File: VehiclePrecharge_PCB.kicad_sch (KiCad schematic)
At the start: 43 parts, among them J1 USB_B, J2 Conn_01x02, J3 Conn_01x02, J4 Main, J5 Conn_01x02, K1 2-1904058-5, Q1 BC847BS, Q2 SSM3J328R LF, SW1 SW_SPDT, U12 LT218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

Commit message: More schematic completed
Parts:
- removed J2, J3: Conn_01x02, symbol Connector_Generic:Conn_01x02
- R11: value 3k -> 10k
- R7: value 220R -> R_small
- U12, U4: value LT218 -> AQY212
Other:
- sheet PWM Economizer1 ports: added Control; removed none
- sheet PWM Economizer2 ports: added Control; removed none
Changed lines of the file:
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@@
     (effects (font (size 1.27 1.27)) (justify left bottom))
-  )
-  (global_label "Shutdown Loop" (shape input) (at 365.76 172.72 180) (fields_autoplaced)
-    (effects (font (size 1.27 1.27)) (justify right))
-    (property "Intersheetrefs" "${INTERSHEET_REFS}" (at 348.6064 172.72 0)
-      (effects (font (size 1.27 1.27)) (justify right) hide)
-    )
   )
   (global_label "SD GND" (shape bidirectional) (at 100.33 204.47 180) (fields_autoplaced)
@@
     )
   )
-  (global_label "AIR- Control" (shape input) (at 274.32 175.26 180) (fields_autoplaced)
+  (global_label "AIR- Control" (shape input) (at 288.29 175.26 180) (fields_autoplaced)
     (effects (font (size 1.27 1.27)) (justify right))
-    (property "Intersheetrefs" "${INTERSHEET_REFS}" (at 259.2223 175.26 0)
+    (property "Intersheetrefs" "${INTERSHEET_REFS}" (at 273.1923 175.26 0)
       (effects (font (size 1.27 1.27)) (justify right) hide)
     )
@@
     )
   )
-  (global_label "Shutdown Loop" (shape input) (at 365.76 151.13 180) (fields_autoplaced)
-    (effects (font (size 1.27 1.27)) (justify right))
-    (property "Intersheetrefs" "${INTERSHEET_REFS}" (at 348.6064 151.13 0)
-      (effects (font (size 1.27 1.27)) (justify right) hide)
-    )
-  )
   (global_label "ALV+" (shape input) (at 38.1 198.12 180) (fields_autoplaced)
     (effects (font (size 1.27 1.27)) (justify right))
@@
     )
   )
-  (global_label "AIR+ Control" (shape input) (at 274.32 152.4 180) (fields_autoplaced)
+  (global_label "AIR+ Control" (shape input) (at 288.29 152.4 180) (fields_autoplaced)
     (effects (font (size 1.27 1.27)) (justify right))
-    (property "Intersheetrefs" "${INTERSHEET_REFS}" (at 259.2223 152.4 0)
+    (property "Intersheetrefs" "${INTERSHEET_REFS}" (at 273.1923 152.4 0)
       (effects (font (size 1.27 1.27)) (justify right) hide)
     )
@@
       (effects (font (size 1.27 1.27)) (justify left))
     )
-    (property "Value" "220R" (at 38.1 269.875 0)
+    (property "Value" "R_small" (at 38.1 269.875 0)
       (effects (font (size 1.27 1.27)) (justify left))
     )
@@
         (path "/3146712d-38b0-45c4-b96b-45a0a31bd3ed"
           (reference "R7") (unit 1)
-        )
-      )
-    )
-  )
-  (symbol (lib_id "Connector_Generic:Conn_01x02") (at 370.84 151.13 0) (unit 1)
-    (in_bom yes) (on_board yes) (dnp no) (fields_autoplaced)
-    (property "Reference" "J2" (at 373.38 151.765 0)
-      (effects (font (size 1.27 1.27)) (justify left))
-    )
-    (property "Value" "Conn_01x02" (at 373.38 154.305 0)
-      (effects (font (size 1.27 1.27)) (justify left))
-    )
-    (property "Footprint" "" (at 370.84 151.13 0)
-      (effects (font (size 1.27 1.27)) hide)
-    )
-    (property "Datasheet" "~" (at 370.84 151.13 0)
-      (effects (font (size 1.27 1.27)) hide)
-    )
-    (pin "1")
-    (pin "2")
-    (instances
-      (project "VehiclePrecharge_PCB"
-        (path "/3146712d-38b0-45c4-b96b-45a0a31bd3ed"
-          (reference "J2") (unit 1)
         )
       )
@@
       (effects (font (size 1.27 1.27)))
     )
-    (property "Value" "LT218" (at 279.4 60.96 0)
+    (property "Value" "AQY212" (at 279.4 60.96 0)
       (effects (font (size 1.27 1.27)))
     )
@@
         (path "/e63e39d7-6ac0-4ffd-8aa3-1841a4541b55"
           (reference "D7") (unit 1)
-        )
-      )
-    )
-  )
-  (symbol (lib_id "Connector_Generic:Conn_01x02") (at 370.84 172.72 0) (unit 1)
-    (in_bom yes) (on_board yes) (dnp no) (fields_autoplaced)
-    (property "Reference" "J3" (at 373.38 173.355 0)
-      (effects (font (size 1.27 1.27)) (justify left))
-    )
-    (property "Value" "Conn_01x02" (at 373.38 175.895 0)
-      (effects (font (size 1.27 1.27)) (justify left))
-    )
-    (property "Footprint" "" (at 370.84 172.72 0)
-      (effects (font (size 1.27 1.27)) hide)
-    )
-    (property "Datasheet" "~" (at 370.84 172.72 0)
-      (effects (font (size 1.27 1.27)) hide)
-    )
-    (pin "1")
-    (pin "2")
-    (instances
-      (project "VehiclePrecharge_PCB"
-        (path "/3146712d-38b0-45c4-b96b-45a0a31bd3ed"
-          (reference "J3") (unit 1)
         )
       )
@@
       (effects (font (size 1.27 1.27)))
     )
-    (property "Value" "3k" (at 158.75 53.34 90)
+    (property "Value" "10k" (at 158.75 53.34 90)
       (effects (font (size 1.27 1.27)))
     )
@@
       (effects (font (size 1.27 1.27)))
     )
-    (property "Value" "LT218" (at 45.72 255.27 0)
+    (property "Value" "AQY212" (at 45.72 255.27 0)
       (effects (font (size 1.27 1.27)))
     )
@@
       (effects (font (size 1.27 1.27)) (justify left top))
     )
+    (pin "Control" input (at 288.29 175.26 180)
+      (effects (font (size 1.27 1.27)) (justify left))
+    )
     (instances
       (project "VehiclePrecharge_PCB"
@@
       (effects (font (size 1.27 1.27)) (justify left top))
     )
-    (instances
+    (pin "Control" input (at 288.29 152.4 180)
+      (effects (font (size 1.27 1.27)) (justify left))
+    )
+    (instances

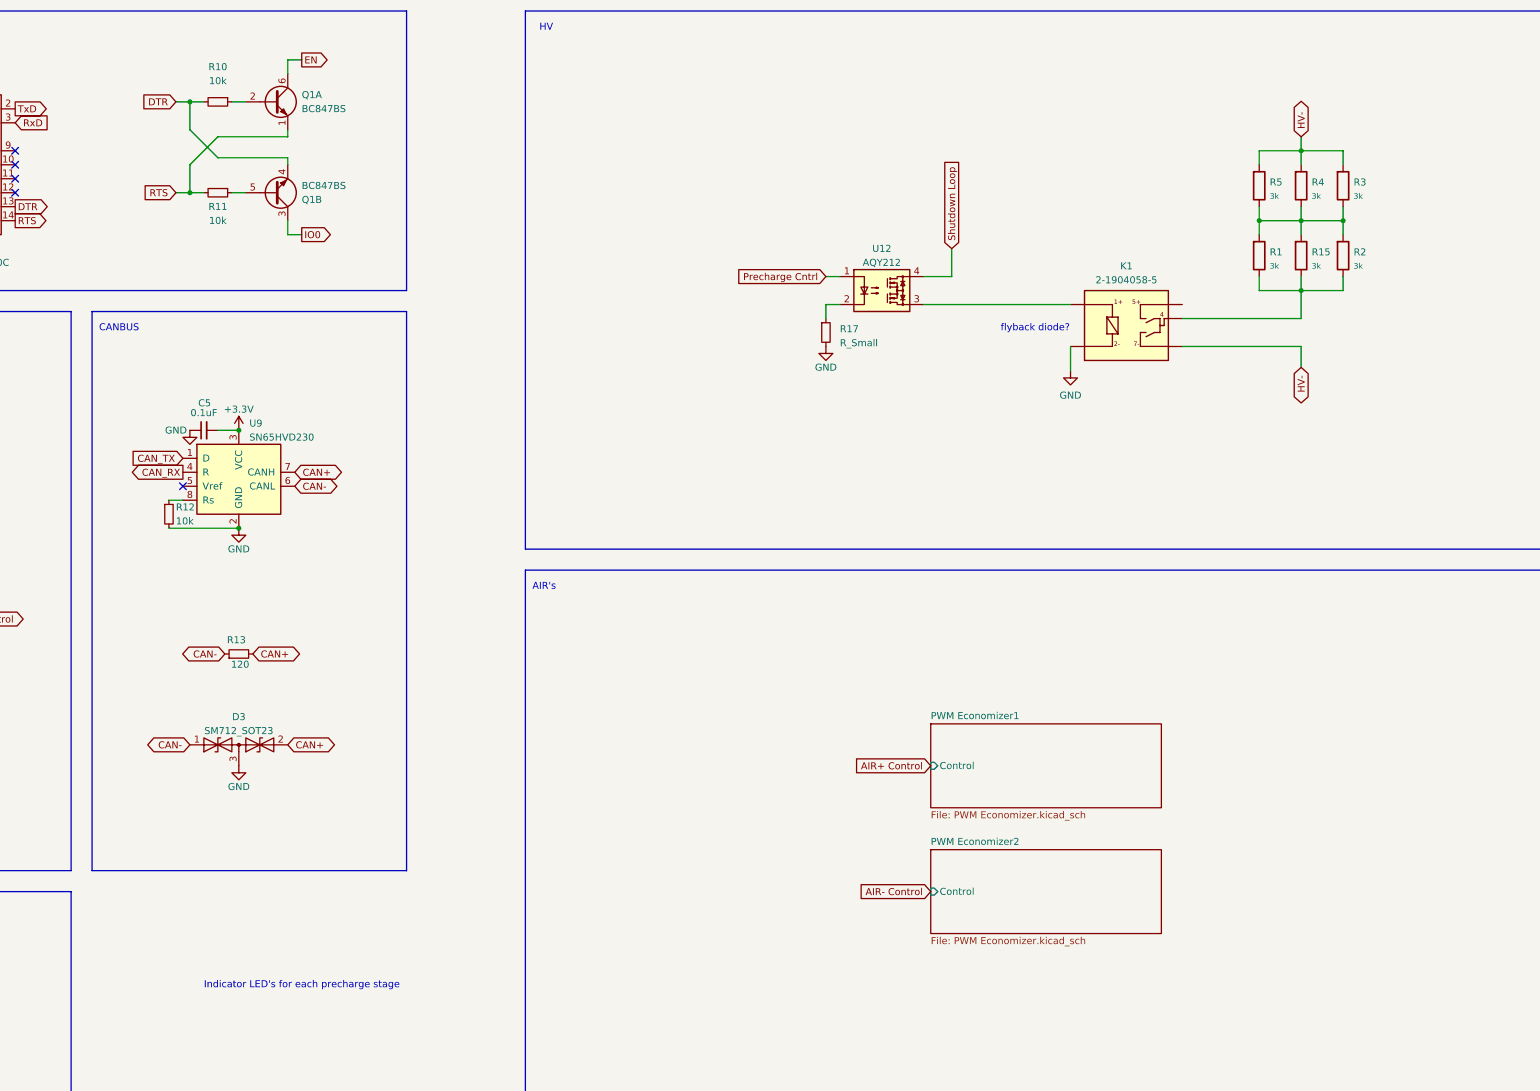
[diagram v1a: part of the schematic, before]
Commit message: Changed to DRV110A
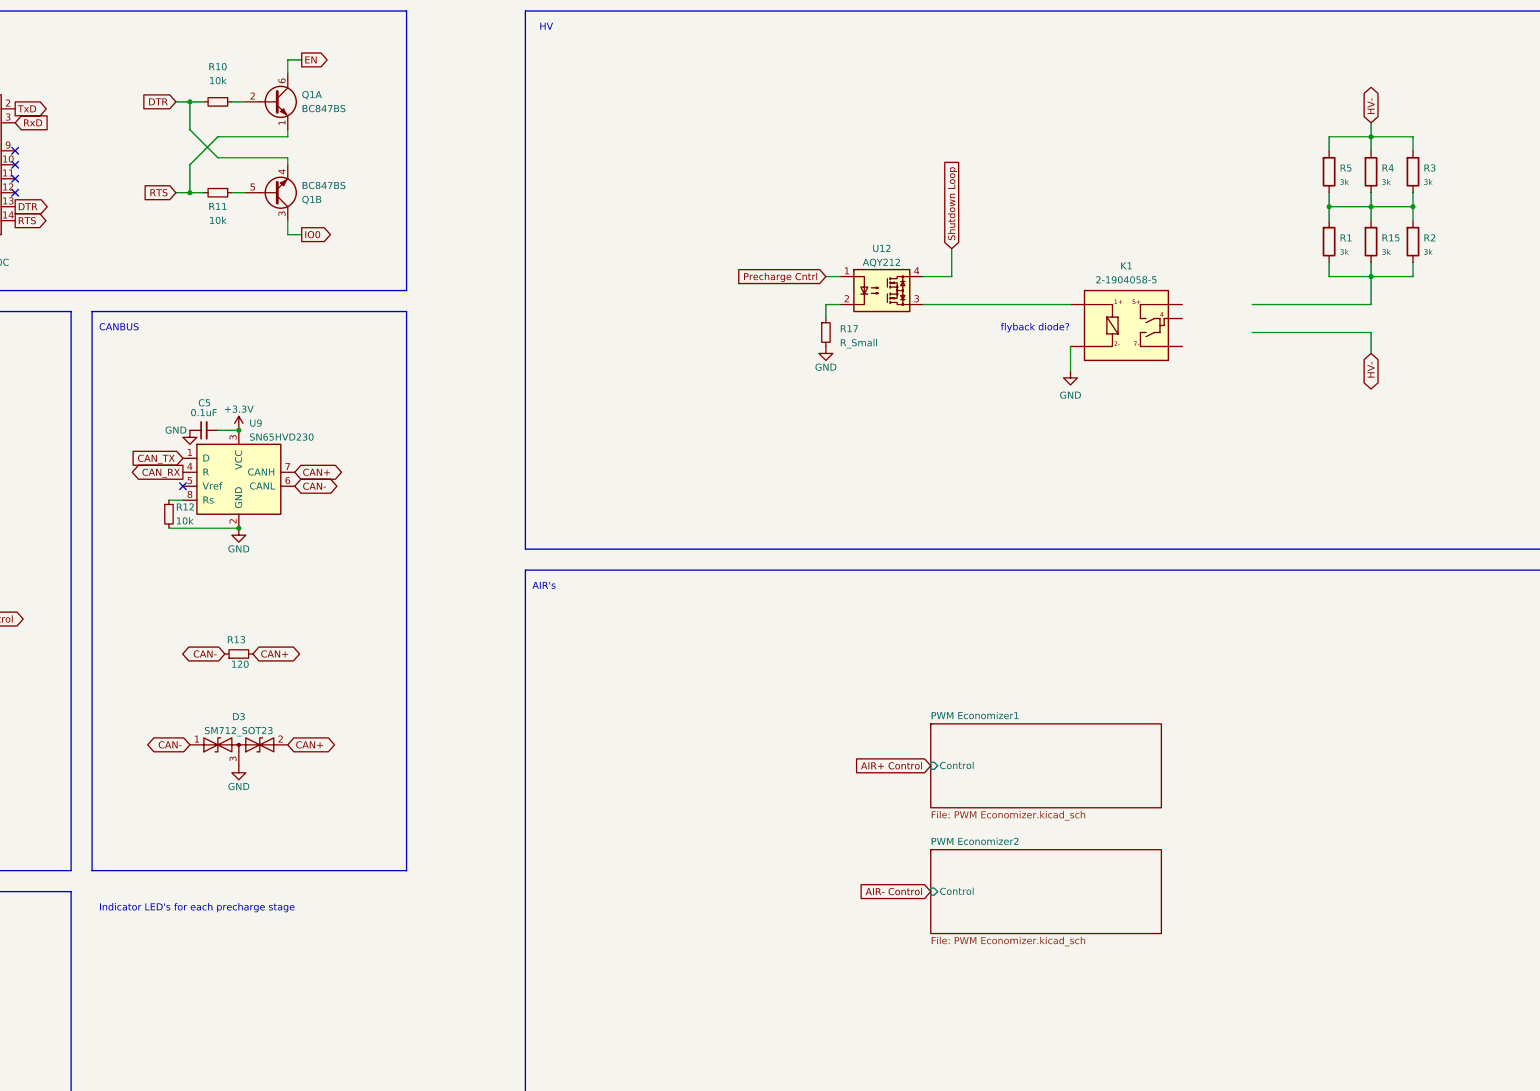
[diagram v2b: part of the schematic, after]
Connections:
- net HV-: no longer K1.7
- net at R1.2, R15.2, R2.2: no longer K1.4
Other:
- moved on the sheet: R1, R15, R2, R3, R4, R5
